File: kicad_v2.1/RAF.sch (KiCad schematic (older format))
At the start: 44 parts, among them J1 SERVO, J2 SERVO, J3 SOL, J4 SERVO, J5 PUMP, J6 WS2811-OUT, J7 I2C, P1 Power, P2 Analog, P3 Digital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

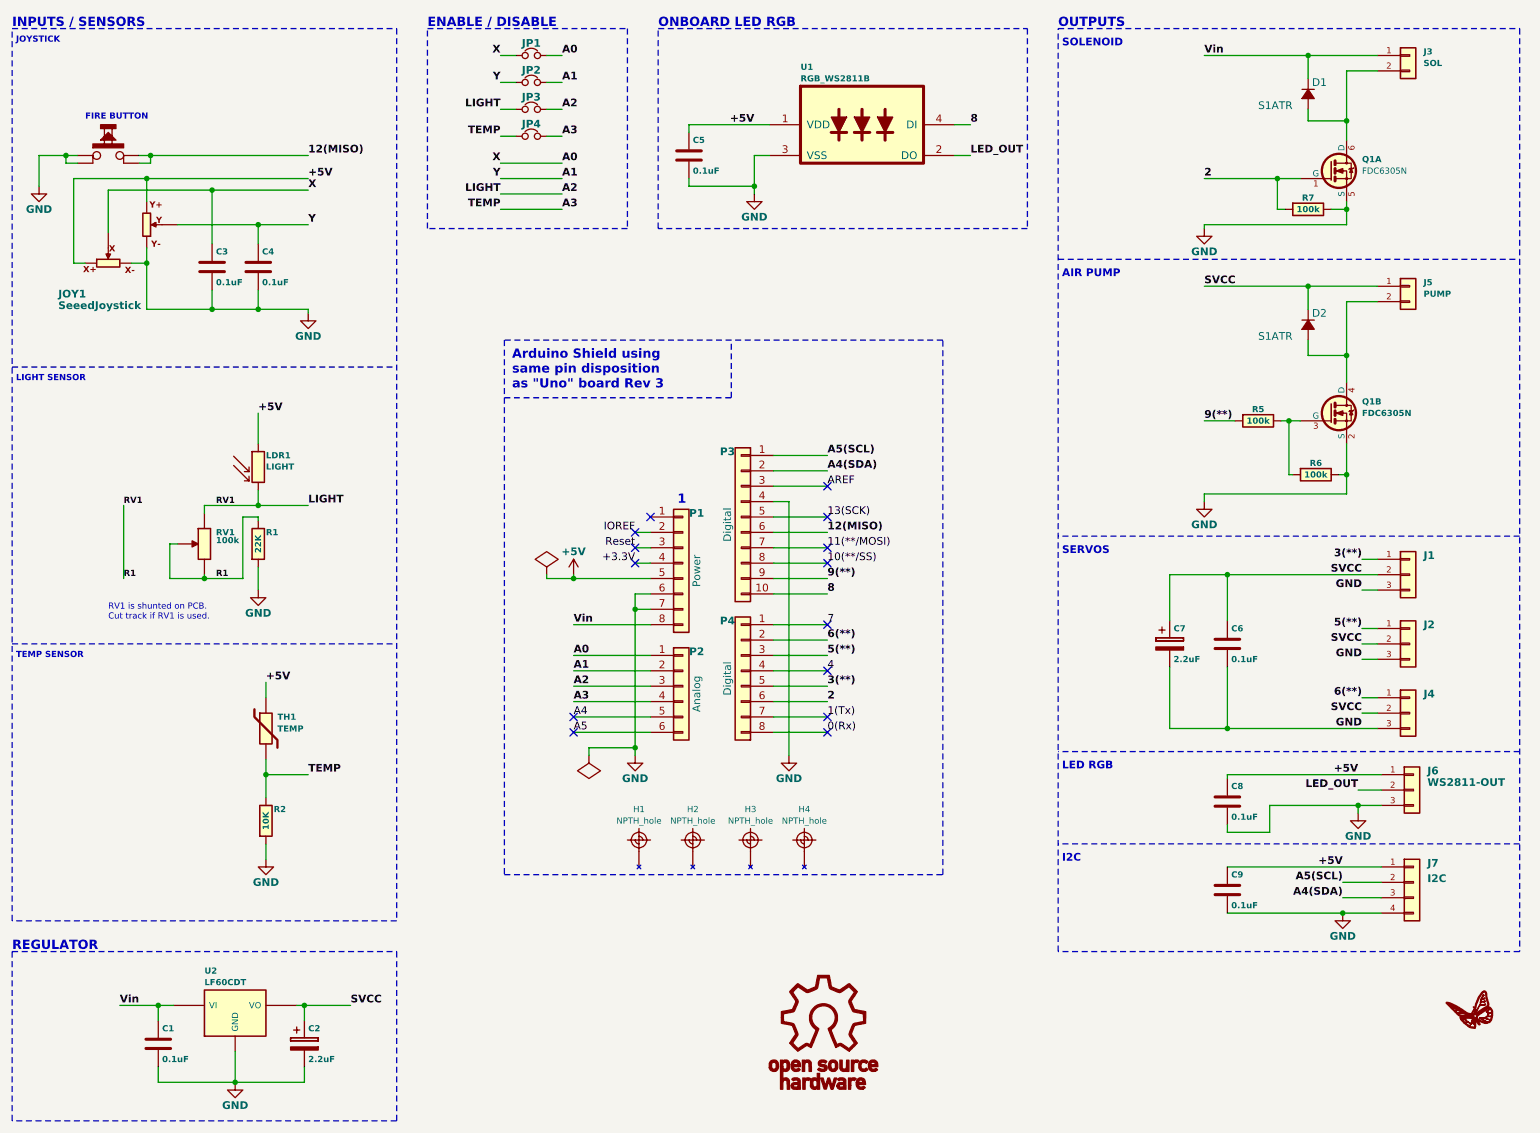
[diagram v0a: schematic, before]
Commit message: added pogo connector for testing solenoid, pump, servo
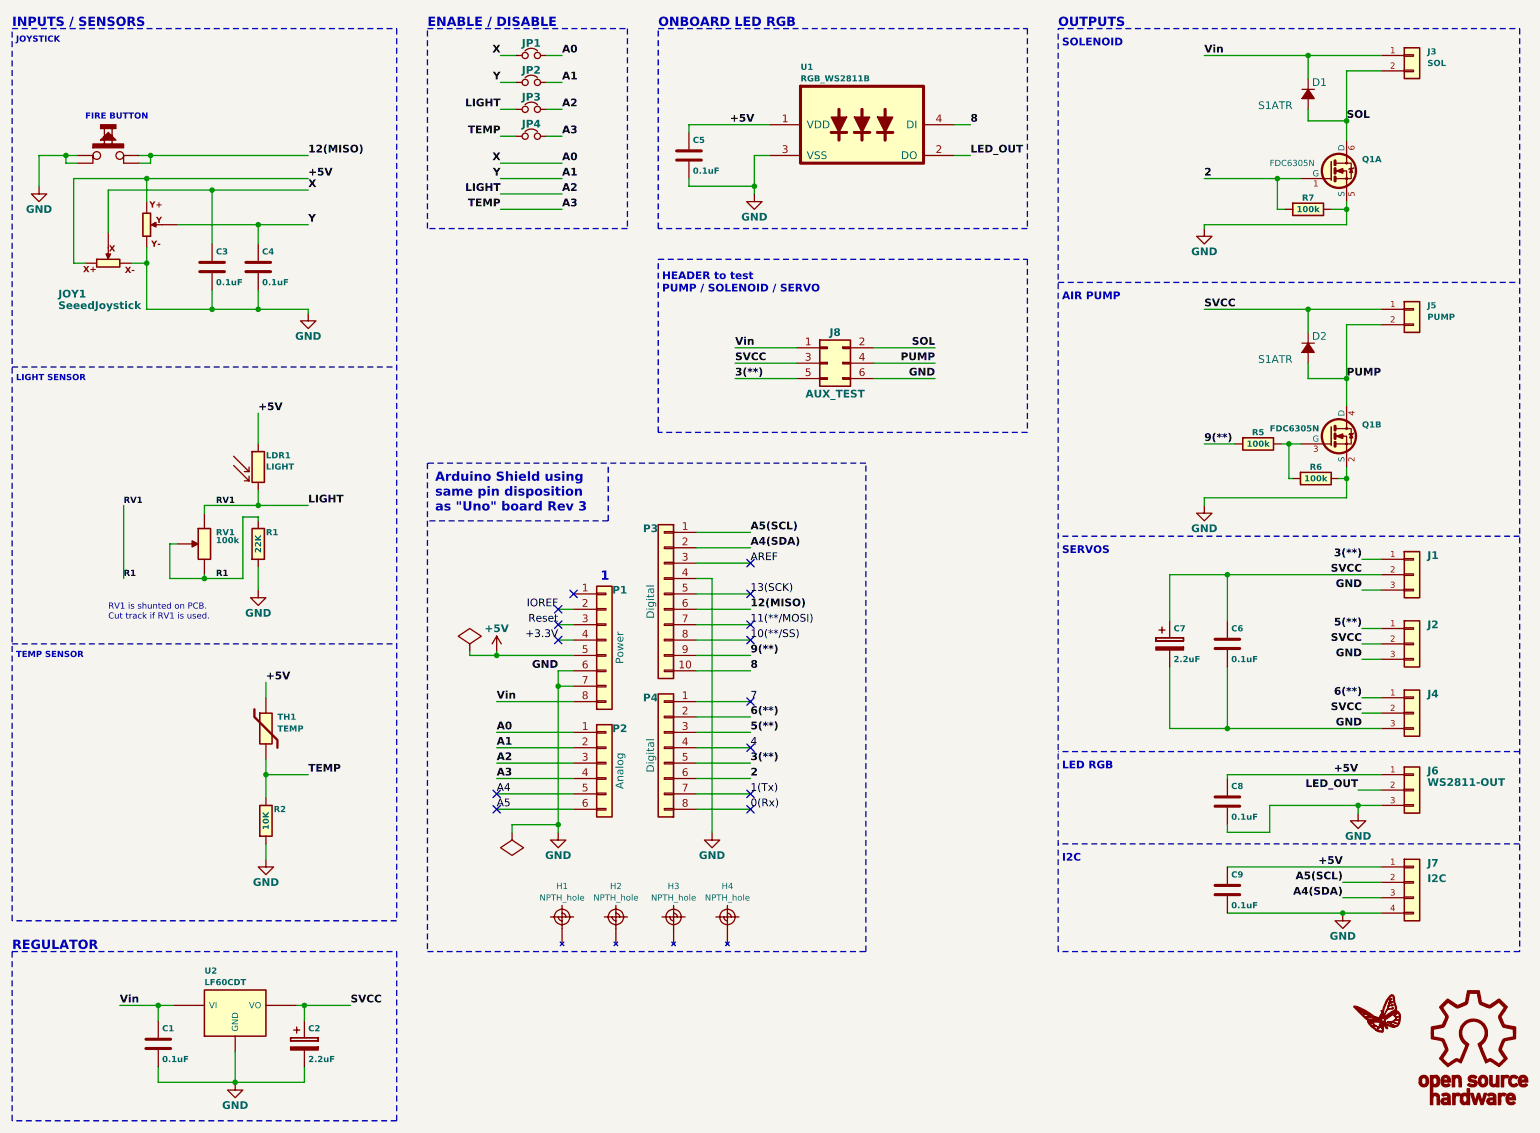
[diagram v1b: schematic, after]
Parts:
- added J8: AUX_TEST, RAF_Libs:TC2030-IDC, symbol CONN_02X03
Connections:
- net 3(**): now also J8.5 (P5)
- net GND: now also J8.6 (P6)
- net SVCC: now also J8.3 (P3)
- net Vin: now also J8.1 (P1)
- net SOL: now reaches D1.2 (A), J3.2 (P2), Q1.6 (D)
- net SOL: now also J8.2 (P2)
- net PUMP: now reaches D2.2 (A), J5.2 (P2), Q1.4 (D)
- net PUMP: now also J8.4 (P4)
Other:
- note added: "HEADER to test\nPUMP / SOLENOID / SERVO"
- moved on the sheet: D2, H1, H2, H3, H4, J1, J2, J3, J4, J5, P1, P2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

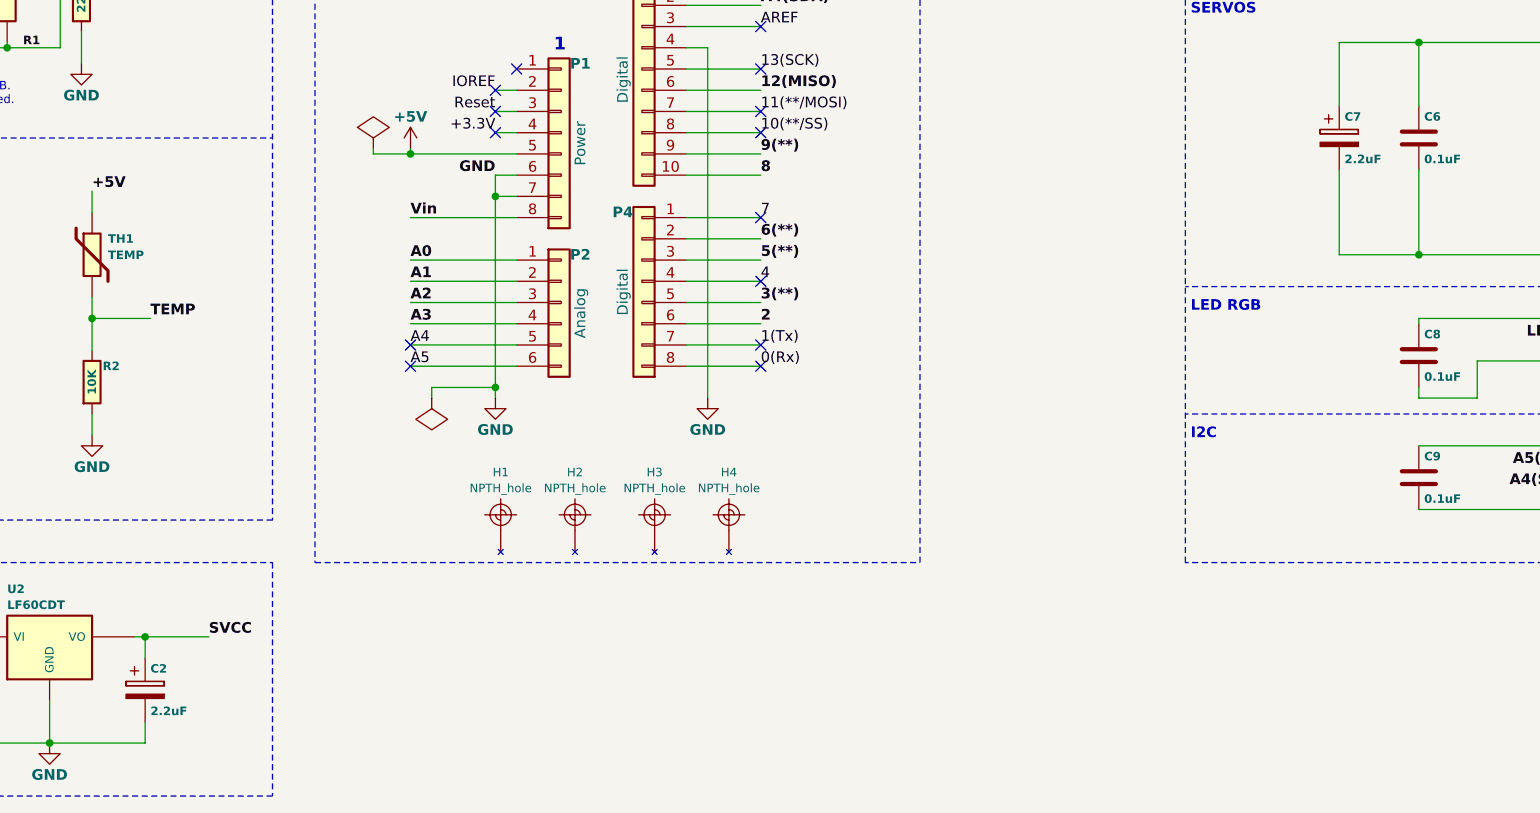
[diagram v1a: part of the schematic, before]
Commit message: edited values of C2,C7
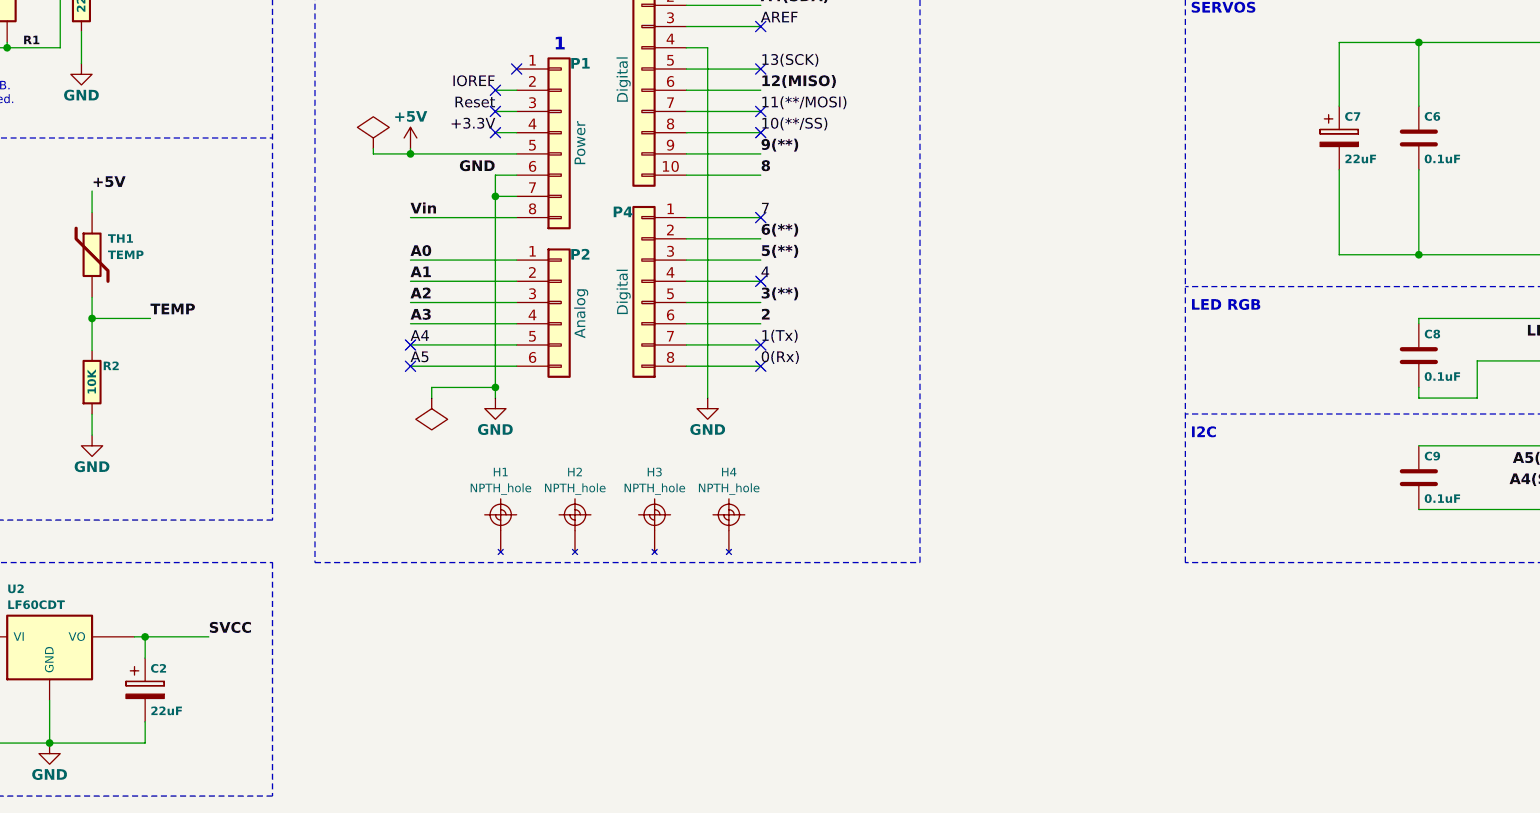
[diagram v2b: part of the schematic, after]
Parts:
- C2, C7: value 2.2uF -> 22uF
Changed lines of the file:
@@
 LIBS:RAF
 LIBS:power
-LIBS:conn
 LIBS:RAF-cache
 EELAYER 25 0
@@
 P 2500 7200
 F 0 "C2" H 2525 7300 40  0000 L CNB
-F 1 "2.2uF" H 2525 7100 40  0000 L CNB
+F 1 "22uF" H 2525 7100 40  0000 L CNB
 F 2 "RAF_Libs:CP_Elec_4x5.7" H 2538 7050 50  0001 C CNN
 F 3 "" H 2500 7200 50  0001 C CNN
@@
 P 8125 4600
 F 0 "C7" H 8150 4700 40  0000 L CNB
-F 1 "2.2uF" H 8150 4500 40  0000 L CNB
+F 1 "22uF" H 8150 4500 40  0000 L CNB
 F 2 "RAF_Libs:CP_Elec_4x5.7" H 8163 4450 50  0001 C CNN
 F 3 "" H 8125 4600 50  0001 C CNN
